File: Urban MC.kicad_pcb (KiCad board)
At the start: 4 copper layers, 166.4 x 118.7 mm, 74 parts, among them J1 Conn_01x02, J2 Conn_01x02, J3 Conn_01x03, J4 Conn_01x02, Q1 IQE022N06LM5CGSCATMA1, Q10 IQE022N06LM5CGSCATMA1, Q11 IQE022N06LM5CGSCATMA1, Q12 IQE022N06LM5CGSCATMA1, Q13 IQE022N06LM5CGSCATMA1, Q14 IQE022N06LM5CGSCATMA1, Q15 IQE022N06LM5CGSCATMA1, Q16 IQE022N06LM5CGSCATMA1, Q17 IQE022N06LM5CGSCATMA1, Q18 IQE022N06LM5CGSCATMA1, Q19 IQE022N06LM5CGSCATMA1, Q2 IQE022N06LM5CGSCATMA1, Q20 IQE022N06LM5CGSCATMA1, Q21 IQE022N06LM5CGSCATMA1, Q22 IQE022N06LM5CGSCATMA1, Q23 IQE022N06LM5CGSCATMA1, Q24 IQE022N06LM5CGSCATMA1, Q3 IQE022N06LM5CGSCATMA1, Q4 IQE022N06LM5CGSCATMA1, Q5 IQE022N06LM5CGSCATMA1, Q6 IQE022N06LM5CGSCATMA1, Q7 IQE022N06LM5CGSCATMA1, Q8 IQE022N06LM5CGSCATMA1, Q9 IQE022N06LM5CGSCATMA1, SW1 CAN_TERM, SW2 SW_Push, U1 MCP2561/2, U2 MCP4725, U3 MCP2515-xSO, Y1 8MHz

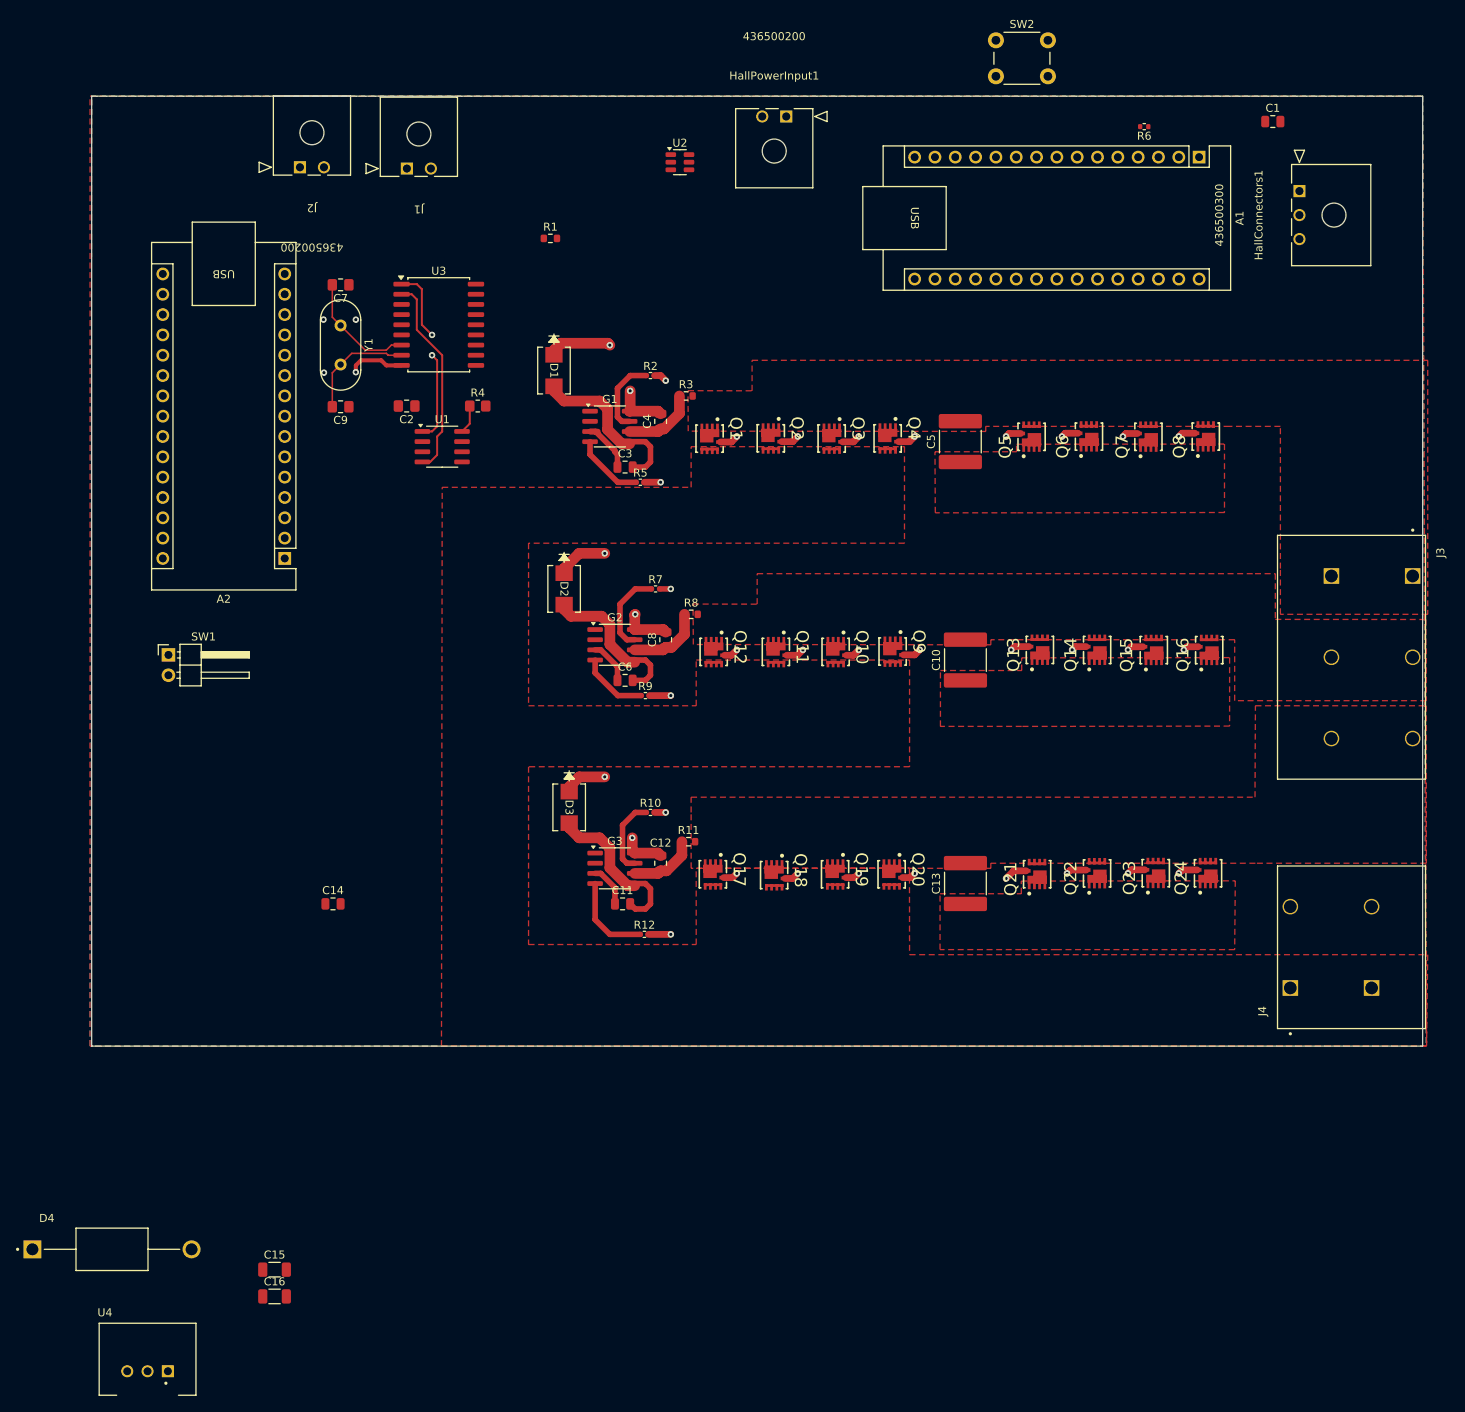
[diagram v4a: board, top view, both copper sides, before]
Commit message: CAN circuit and voltage regulator first draft, mounting holes
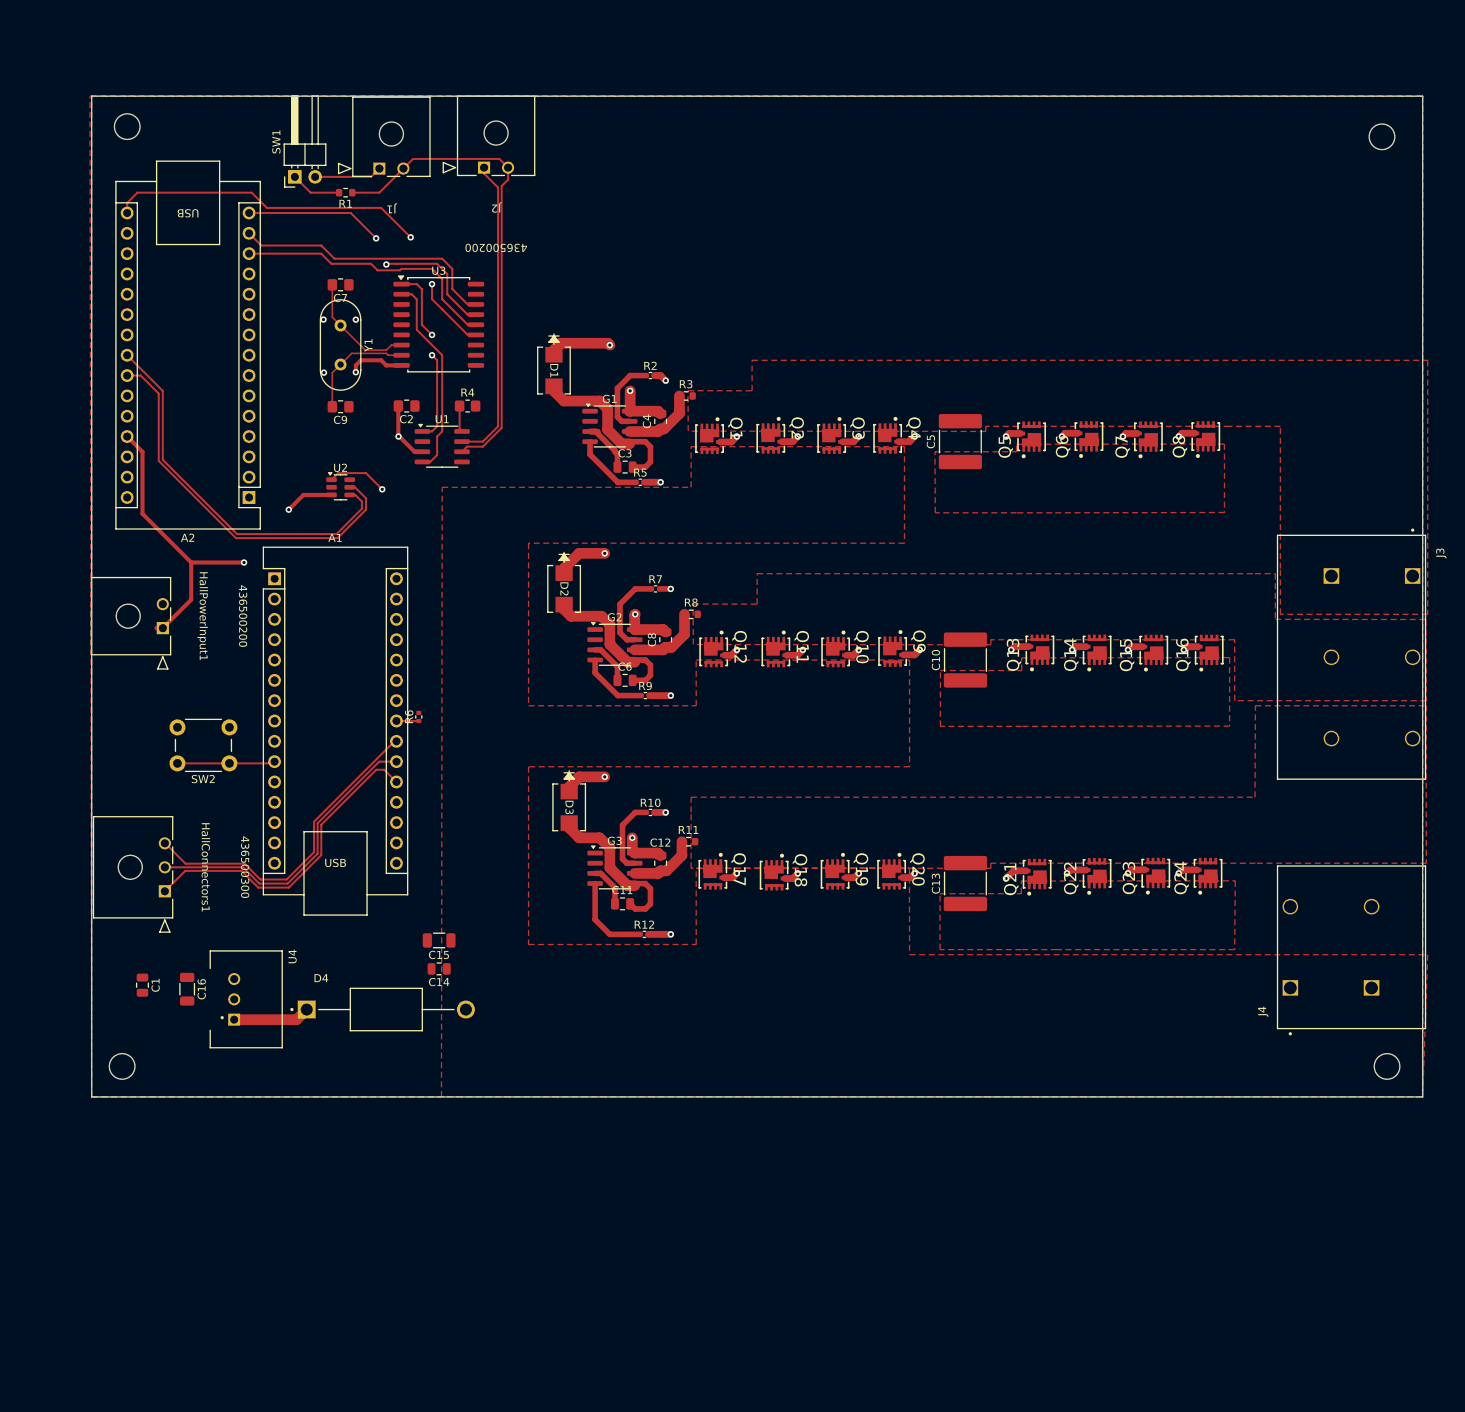
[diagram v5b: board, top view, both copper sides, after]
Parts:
- added REF**: MountingHole_3.2mm_M3, MountingHole:MountingHole_3.2mm_M3, F.Cu at (96.5, 149.9)
- added REF**: MountingHole_3.2mm_M3, MountingHole:MountingHole_3.2mm_M3, F.Cu at (254.0, 33.7)
- added REF**: MountingHole_3.2mm_M3, MountingHole:MountingHole_3.2mm_M3, F.Cu at (97.2, 32.4)
- added REF**: MountingHole_3.2mm_M3, MountingHole:MountingHole_3.2mm_M3, F.Cu at (254.6, 149.9)
- moved C1 177.8 mm to (99.1, 139.7), turned to -90 degrees
- moved HallConnectors1 166.7 mm to (101.9, 128.0), turned to -90 degrees
- moved SW2 131.7 mm to (109.9, 112.0), turned to 180 degrees
- moved A1 127.0 mm to (115.6, 88.9), turned to 0 degrees
- moved R6 116.9 mm to (133.6, 106.2), turned to 90 degrees
- moved HallPowerInput1 100.8 mm to (101.6, 95.1), turned to -90 degrees
- moved SW1 61.8 mm to (118.1, 38.7), turned to 90 degrees
- moved U2 58.7 mm to (123.8, 77.5)
- moved U4 46.4 mm to (112.8, 141.2), turned to 90 degrees
- moved C15 46.0 mm to (136.1, 134.1), turned to 180 degrees
- moved D4 45.5 mm to (129.5, 142.7)
- moved C16 39.9 mm to (104.6, 140.2), turned to -90 degrees
- moved R1 26.2 mm to (124.5, 40.6), turned to 180 degrees
- moved J2 23.0 mm to (141.8, 37.5)
- moved C14 15.6 mm to (136.1, 137.7), turned to 180 degrees
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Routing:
- net +5V: track 0.00 -> 101.8 mm, vias 0 -> 3
- net /CAN LOW: track 0.00 -> 60.7 mm
- net SCK: track 0.00 -> 55.7 mm, vias 0 -> 2
- net /A5: track 0.00 -> 48.7 mm
- net /A4: track 0.00 -> 47.7 mm
- net /HALL A: track 0.00 -> 40.2 mm
- net /THROTTLE: track 0.00 -> 40.0 mm, vias 0 -> 1
- net /HALL C: track 0.00 -> 39.8 mm
- net /CAN HIGH: track 0.00 -> 38.4 mm
- net /HALL B: track 0.00 -> 38.3 mm
- net SO: track 0.00 -> 36.4 mm, vias 0 -> 2
- net CS: track 0.00 -> 33.7 mm
- net SI: track 0.00 -> 33.5 mm
- net Net-(A1-D7): track 0.00 -> 12.2 mm
- net Net-(U4-VIN): track 0.00 -> 9.59 mm
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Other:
- board size 166.4 x 118.7 mm -> 166.4 x 125.1 mm

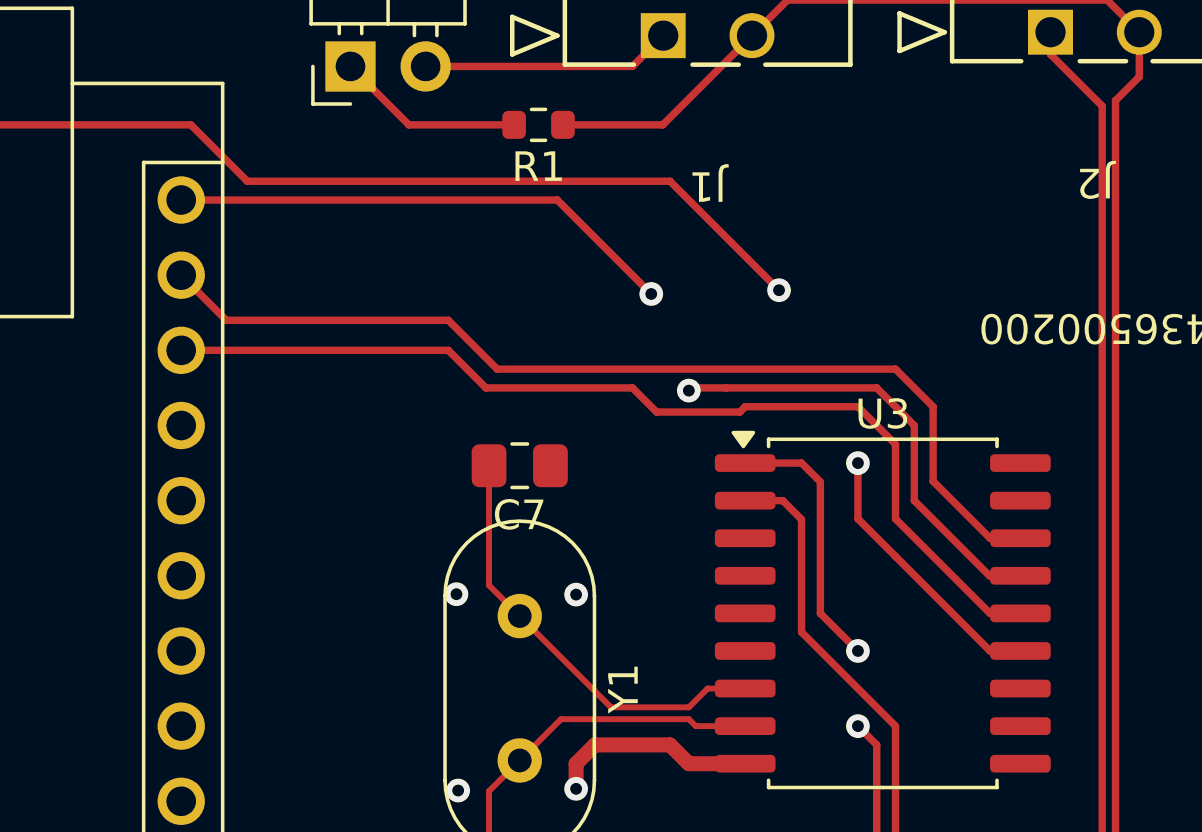
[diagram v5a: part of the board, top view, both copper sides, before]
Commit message: small trace edits
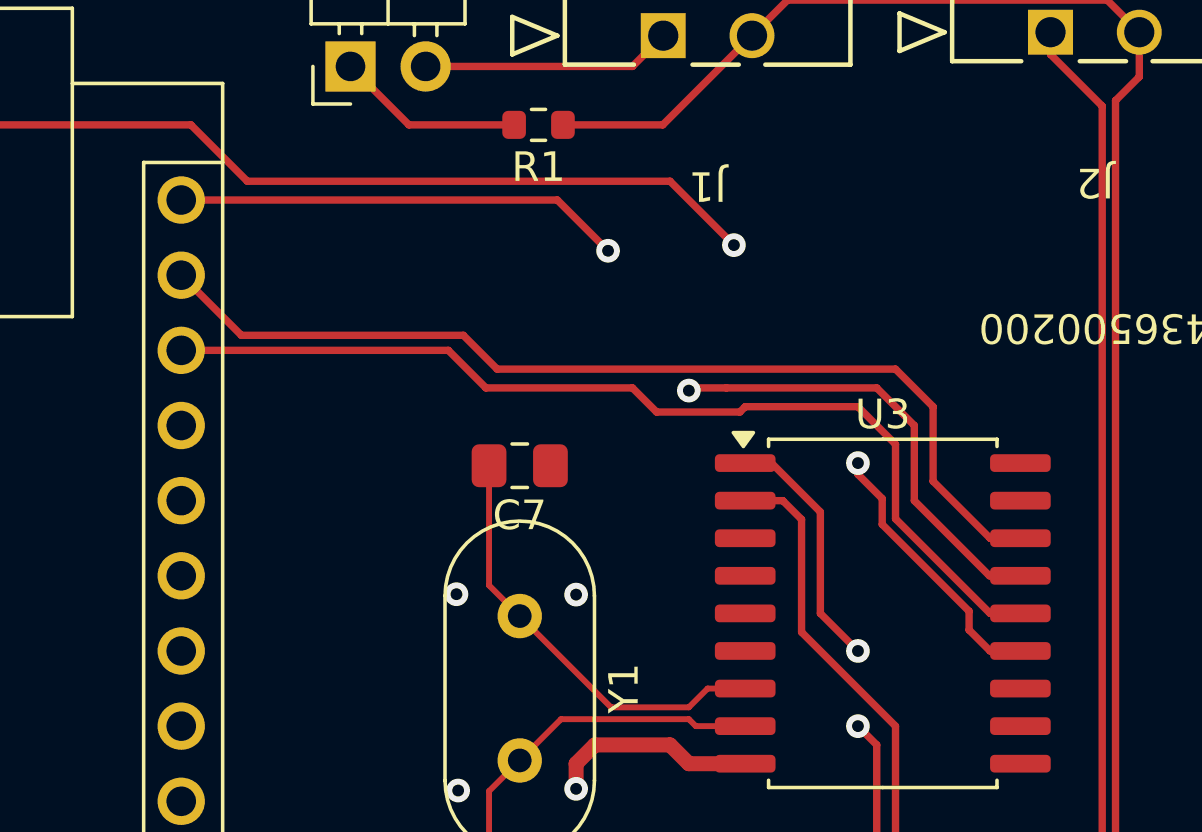
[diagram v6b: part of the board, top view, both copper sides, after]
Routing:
- net Net-(U1-TXD): track 22.8 -> 22.2 mm
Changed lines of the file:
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@@
 		(tags "Arduino Nano")
 		(property "Reference" "A1"
-			(at 7.62 -5.08 360)
+			(at 7.62 -5.08 0)
 			(layer "F.SilkS")
 			(effects
@@
 		(tags "tact sw push 6mm")
 		(property "Reference" "SW2"
-			(at 3.25 -2 360)
+			(at 3.25 -2 0)
 			(layer "F.SilkS")
 			(effects
@@
 		)
 		(property "Value" "SW_Push"
-			(at 3.75 6.7 360)
+			(at 3.75 6.7 0)
 			(layer "F.Fab")
 			(effects
@@
 		)
 		(fp_text user "${REFERENCE}"
-			(at 3.25 2.25 360)
+			(at 3.25 2.25 0)
 			(layer "F.Fab")
 			(effects
@@
 		)
 		(fp_text user "${REFERENCE}"
-			(at 2.77 1.27 360)
+			(at 2.77 1.27 0)
 			(layer "F.Fab")
 			(effects
@@
 		(tags "resistor")
 		(property "Reference" "R1"
-			(at 0 -1.43 360)
+			(at 0 -1.43 0)
 			(layer "F.SilkS")
 			(effects
@@
 		)
 		(property "Value" "120"
-			(at 0 1.43 360)
+			(at 0 1.43 0)
 			(layer "F.Fab")
 			(effects
@@
 		)
 		(fp_text user "${REFERENCE}"
-			(at 0 0 360)
+			(at 0 0 0)
 			(layer "F.Fab")
 			(effects
@@
 		(tags "capacitor")
 		(property "Reference" "C15"
-			(at 0 -1.85 360)
+			(at 0 -1.85 0)
 			(layer "F.SilkS")
 			(effects
@@
 		)
 		(property "Value" "1u"
-			(at 0 1.85 360)
+			(at 0 1.85 0)
 			(layer "F.Fab")
 			(effects
@@
 		)
 		(fp_text user "${REFERENCE}"
-			(at 0 0 360)
+			(at 0 0 0)
 			(layer "F.Fab")
 			(effects
@@
 		(tags "capacitor")
 		(property "Reference" "C14"
-			(at 0 -1.68 360)
+			(at 0 -1.68 0)
 			(layer "F.SilkS")
 			(effects
@@
 		)
 		(property "Value" "10u"
-			(at 0 1.68 360)
+			(at 0 1.68 0)
 			(layer "F.Fab")
 			(effects
@@
 		)
 		(fp_text user "${REFERENCE}"
-			(at 0 0 360)
+			(at 0 0 0)
 			(layer "F.Fab")
 			(effects
@@
 		(at 129.54 142.748)
 		(property "Reference" "D4"
-			(at -8.15 -3.885 360)
+			(at -8.15 -3.885 0)
 			(layer "F.SilkS")
 			(effects
@@
 		)
 		(property "Value" "D"
-			(at 2.01 3.885 360)
+			(at 2.01 3.885 0)
 			(layer "F.Fab")
 			(effects
@@
 		)
 		(property "Footprint" "urban_mc_custom_footprints:DO-201AD"
-			(at 0 0 360)
+			(at 0 0 0)
 			(layer "F.Fab")
 			(hide yes)
@@
 		)
 		(property "Datasheet" "https://services.taiwansemi.com/storage/resources/datasheet/SR1202%20SERIES_G2105.pdf"
-			(at 0 0 360)
+			(at 0 0 0)
 			(layer "F.Fab")
 			(hide yes)
@@
 		)
 		(property "Description" ""
-			(at 0 0 360)
+			(at 0 0 0)
 			(layer "F.Fab")
 			(hide yes)
@@
 	)
 	(segment
-		(start 136.535001 55.234999)
-		(end 136.525 55.224999)
+		(start 128.905 42.545)
+		(end 114.6175 42.545)
 		(width 0.25)
 		(layer "F.Cu")
@@
 	)
 	(segment
-		(start 114.6175 42.545)
-		(end 112.7125 40.64)
+		(start 98.425 40.64)
+		(end 97.145 41.92)
 		(width 0.25)
 		(layer "F.Cu")
@@
 	)
 	(segment
-		(start 98.425 40.64)
-		(end 97.145 41.92)
+		(start 139.010803 57.710802)
+		(end 139.720001 58.42)
 		(width 0.25)
 		(layer "F.Cu")
@@
 	)
 	(segment
-		(start 132.588 46.228)
-		(end 128.905 42.545)
+		(start 139.720001 58.42)
+		(end 140.745 58.42)
 		(width 0.25)
 		(layer "F.Cu")
@@
 	)
 	(segment
-		(start 139.720001 58.42)
-		(end 136.535001 55.234999)
+		(start 135.255 52.451)
+		(end 136.075 53.271)
 		(width 0.25)
 		(layer "F.Cu")
@@
 	)
 	(segment
-		(start 128.905 42.545)
-		(end 114.6175 42.545)
+		(start 136.075 54.141395)
+		(end 139.010803 57.077198)
 		(width 0.25)
 		(layer "F.Cu")
@@
 	)
 	(segment
-		(start 135.255 53.954998)
-		(end 135.255 52.07)
+		(start 139.010803 57.077198)
+		(end 139.010803 57.710802)
 		(width 0.25)
 		(layer "F.Cu")
@@
 	)
 	(segment
-		(start 140.745 58.42)
-		(end 139.720001 58.42)
+		(start 131.064 44.704)
+		(end 128.905 42.545)
+		(width 0.25)
+		(layer "F.Cu")
+		(net 32)
+	)
+	(segment
+		(start 136.075 53.271)
+		(end 136.075 54.141395)
+		(width 0.25)
+		(layer "F.Cu")
+		(net 32)
+	)
+	(segment
+		(start 114.6175 42.545)
+		(end 112.7125 40.64)
 		(width 0.25)
 		(layer "F.Cu")
@@
 	)
 	(segment
-		(start 136.535001 55.234999)
-		(end 135.255 53.954998)
+		(start 135.255 52.07)
+		(end 135.255 52.451)
 		(width 0.25)
 		(layer "F.Cu")
@@
 	)
 	(via
-		(at 132.588 46.228)
+		(at 131.064 44.704)
 		(size 0.8)
 		(drill 0.4)
@@
 	)
 	(segment
-		(start 132.588 46.228)
-		(end 135.255 48.895)
+		(start 135.255 48.895)
+		(end 135.255 52.07)
 		(width 0.25)
 		(layer "In2.Cu")
@@
 	)
 	(segment
-		(start 135.255 48.895)
-		(end 135.255 52.07)
+		(start 131.064 44.704)
+		(end 135.255 48.895)
 		(width 0.25)
 		(layer "In2.Cu")
@@
 	)
 	(segment
-		(start 113.909 47.244)
-		(end 112.385 45.72)
+		(start 136.525 48.895)
+		(end 123.063 48.895)
 		(width 0.25)
 		(layer "F.Cu")
@@
 	)
 	(segment
-		(start 140.745 54.61)
-		(end 139.720001 54.61)
+		(start 121.92 47.752)
+		(end 114.417 47.752)
 		(width 0.25)
 		(layer "F.Cu")
@@
 	)
 	(segment
-		(start 139.720001 54.61)
-		(end 137.795 52.684999)
+		(start 114.417 47.752)
+		(end 112.385 45.72)
 		(width 0.25)
 		(layer "F.Cu")
@@
 	)
 	(segment
-		(start 136.525 48.895)
-		(end 123.063 48.895)
+		(start 137.795 52.684999)
+		(end 137.795 50.165)
 		(width 0.25)
 		(layer "F.Cu")
@@
 	)
 	(segment
-		(start 121.412 47.244)
-		(end 113.909 47.244)
+		(start 137.795 50.165)
+		(end 136.525 48.895)
 		(width 0.25)
 		(layer "F.Cu")
@@
 	)
 	(segment
-		(start 137.795 52.684999)
-		(end 137.795 50.165)
+		(start 123.063 48.895)
+		(end 121.92 47.752)
 		(width 0.25)
 		(layer "F.Cu")
@@
 	)
 	(segment
-		(start 137.795 50.165)
-		(end 136.525 48.895)
+		(start 139.720001 54.61)
+		(end 137.795 52.684999)
 		(width 0.25)
 		(layer "F.Cu")
@@
 	)
 	(segment
-		(start 123.063 48.895)
-		(end 121.412 47.244)
+		(start 140.745 54.61)
+		(end 139.720001 54.61)
 		(width 0.25)
 		(layer "F.Cu")
@@
 	)
 	(segment
+		(start 126.8095 44.8945)
+		(end 125.095 43.18)
+		(width 0.25)
+		(layer "F.Cu")
+		(net 45)
+	)
+	(segment
+		(start 125.095 43.18)
+		(end 112.385 43.18)
+		(width 0.25)
+		(layer "F.Cu")
+		(net 45)
+	)
+	(segment
 		(start 135.89 49.53)
 		(end 130.81 49.53)
@@
 	)
 	(segment
-		(start 112.385 43.18)
-		(end 125.095 43.18)
-		(width 0.25)
-		(layer "F.Cu")
-		(net 45)
-	)
-	(segment
 		(start 129.63 49.53)
 		(end 129.54 49.62)
@@
 		(net 45)
 	)
-	(segment
-		(start 125.095 43.18)
-		(end 128.27 46.355)
-		(width 0.25)
-		(layer "F.Cu")
-		(net 45)
-	)
 	(via
 		(at 129.54 49.62)
@@
 	)
 	(via
-		(at 128.27 46.355)
+		(at 126.8095 44.8945)
 		(size 0.8)
 		(drill 0.4)
@@
 	)
 	(segment
-		(start 128.27 46.355)
-		(end 128.27 48.35)
+		(start 126.8095 46.8895)
+		(end 129.54 49.62)
 		(width 0.25)
 		(layer "In2.Cu")
@@
 	)
 	(segment
-		(start 128.27 48.35)
-		(end 129.54 49.62)
+		(start 126.8095 44.8945)
+		(end 126.8095 46.8895)
 		(width 0.25)
 		(layer "In2.Cu")
@@
 	)
 	(segment
-		(start 133.35 52.07)
-		(end 131.445 52.07)
+		(start 133.985 57.15)
+		(end 133.985 53.721)
 		(width 0.25)
 		(layer "F.Cu")
@@
 	)
 	(segment
-		(start 133.985 52.705)
-		(end 133.35 52.07)
+		(start 135.255 58.42)
+		(end 133.985 57.15)
 		(width 0.25)
 		(layer "F.Cu")
@@
 	)
 	(segment
-		(start 134.05 70.485)
-		(end 135.255 70.485)
+		(start 133.985 53.721)
+		(end 132.334 52.07)
 		(width 0.25)
 		(layer "F.Cu")
@@
 	)
 	(segment
-		(start 133.985 57.15)
-		(end 133.985 52.705)
+		(start 134.05 70.485)
+		(end 135.255 70.485)
 		(width 0.25)
 		(layer "F.Cu")
@@
 	)
 	(segment
-		(start 135.255 58.42)
-		(end 133.985 57.15)
+		(start 132.334 52.07)
+		(end 131.445 52.07)
 		(width 0.25)
 		(layer "F.Cu")
